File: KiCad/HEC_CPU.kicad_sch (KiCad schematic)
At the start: 20 parts, among them J3 Conn_02x05_Odd_Even, J9 Conn_02x14_Odd_Even, SW2 SW_Push, U1 Z80CPU, U16 74LS32, U20 74LS574, U21 74LS574, U22 74LS02, U30 74LS74, U34 74LS393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

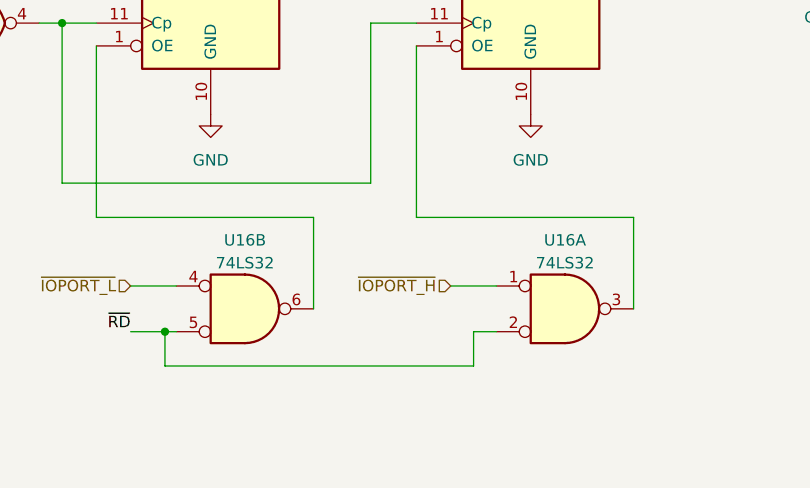
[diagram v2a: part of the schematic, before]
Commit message: Preliminary routing
Changed footprint pad size to allow 2 traces to be routed between adjacent pads. Finished routing all ICs. Bypass caps not added. Some traces may need to be optimized.
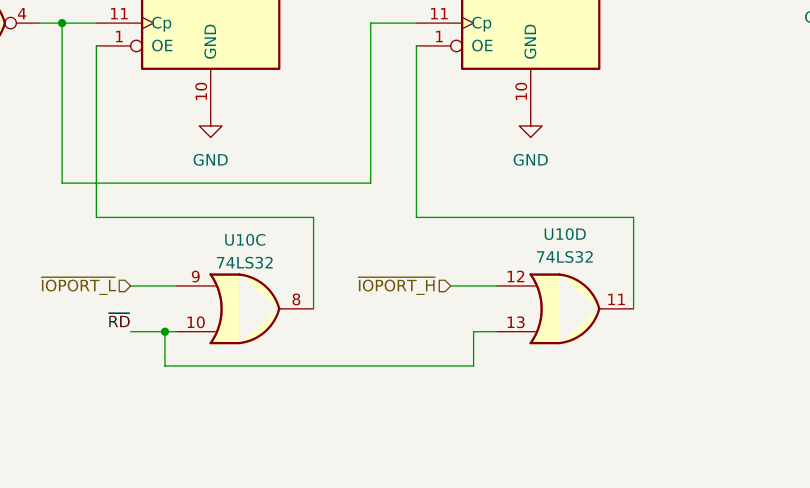
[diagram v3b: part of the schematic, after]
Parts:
- removed U16: 74LS32, Package_DIP:DIP-14_W7.62mm_Socket, symbol 74xx:74LS32
- added U10: 74LS32, Library:DIP-14_W7.62mm_Socket_ThinPads, symbol 74xx:74LS32
- U1: footprint Package_DIP:DIP-40_W15.24mm_Socket -> Library:DIP-40_W15.24mm_Socket_ThinPads
- U20, U21, U36: footprint Package_DIP:DIP-20_W7.62mm_Socket -> Library:DIP-20_W7.62mm_Socket_ThinPads
- U22, U30, U34, U37: footprint Package_DIP:DIP-14_W7.62mm_Socket -> Library:DIP-14_W7.62mm_Socket_ThinPads
- U38, U39: footprint Package_DIP:DIP-16_W7.62mm_Socket -> Library:DIP-16_W7.62mm_Socket_ThinPads
- U7: footprint Package_DIP:DIP-28_W15.24mm_Socket -> Library:DIP-28_W15.24mm_Socket_ThinPads
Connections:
- net ~{IOPORT_H}: now also U10.12
- net ~{IOPORT_L}: now also U10.9
- net ~{RD}: now also U10.10, U10.13
- net at U20.1 (OE): now also U10.8
- net at U21.1 (OE): now also U10.11
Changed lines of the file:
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@@
       (effects (font (size 1.27 1.27)) (justify left))
     )
-    (property "Footprint" "Package_DIP:DIP-16_W7.62mm_Socket" (at 205.105 77.47 0)
+    (property "Footprint" "Library:DIP-16_W7.62mm_Socket_ThinPads" (at 205.105 77.47 0)
       (effects (font (size 1.27 1.27)) hide)
     )
@@
       (effects (font (size 1.27 1.27)) (justify left))
     )
-    (property "Footprint" "Package_DIP:DIP-20_W7.62mm_Socket" (at 110.49 128.27 0)
+    (property "Footprint" "Library:DIP-20_W7.62mm_Socket_ThinPads" (at 110.49 128.27 0)
       (effects (font (size 1.27 1.27)) hide)
     )
@@
       (effects (font (size 1.27 1.27)) (justify left))
     )
-    (property "Footprint" "Package_DIP:DIP-20_W7.62mm_Socket" (at 168.91 52.07 0)
+    (property "Footprint" "Library:DIP-20_W7.62mm_Socket_ThinPads" (at 168.91 52.07 0)
       (effects (font (size 1.27 1.27)) hide)
     )
@@
     )
   )
+  (symbol (lib_id "74xx:74LS32") (at 114.3 170.18 0) (unit 3)
+    (in_bom yes) (on_board yes) (dnp no)
+    (property "Reference" "U10" (at 114.3 162.56 0)
+      (effects (font (size 1.27 1.27)))
+    )
+    (property "Value" "74LS32" (at 114.3 165.1 0)
+      (effects (font (size 1.27 1.27)))
+    )
+    (property "Footprint" "Library:DIP-14_W7.62mm_Socket_ThinPads" (at 114.3 170.18 0)
+      (effects (font (size 1.27 1.27)) hide)
+    )
+    (property "Datasheet" "http://www.ti.com/lit/gpn/sn74LS32" (at 114.3 170.18 0)
+      (effects (font (size 1.27 1.27)) hide)
+    )
+    (pin "1")
+    (pin "2")
+    (pin "3")
+    (pin "4")
+    (pin "5")
+    (pin "6")
+    (pin "10")
+    (pin "8")
+    (pin "9")
+    (pin "11")
+    (pin "12")
+    (pin "13")
+    (pin "14")
+    (pin "7")
+    (instances
+      (project "HEC1"
+        (path "/87935374-b60a-4f41-99da-94b76103dd77/73a0c68b-1e42-4c0d-ae31-b1a96d0648bb"
+          (reference "U10") (unit 3)
+        )
+        (path "/87935374-b60a-4f41-99da-94b76103dd77/2930b625-d6a3-4a7f-9d41-a454efcef99d"
+          (reference "U10") (unit 3)
+        )
+      )
+    )
+  )
   (symbol (lib_id "Oscillator:CXO_DIP8") (at 194.31 148.59 0) (unit 1)
     (in_bom yes) (on_board yes) (dnp no) (fields_autoplaced)
@@
       (effects (font (size 1.27 1.27)))
     )
-    (property "Footprint" "Package_DIP:DIP-14_W7.62mm_Socket" (at 147.32 99.06 0)
+    (property "Footprint" "Library:DIP-14_W7.62mm_Socket_ThinPads" (at 147.32 99.06 0)
       (effects (font (size 1.27 1.27)) hide)
     )
@@
       (effects (font (size 1.27 1.27)))
     )
-    (property "Footprint" "Package_DIP:DIP-14_W7.62mm_Socket" (at 83.82 138.43 0)
+    (property "Footprint" "Library:DIP-14_W7.62mm_Socket_ThinPads" (at 83.82 138.43 0)
       (effects (font (size 1.27 1.27)) hide)
     )
@@
       (effects (font (size 1.27 1.27)))
     )
-    (property "Footprint" "Package_DIP:DIP-14_W7.62mm_Socket" (at 231.775 151.13 0)
+    (property "Footprint" "Library:DIP-14_W7.62mm_Socket_ThinPads" (at 231.775 151.13 0)
       (effects (font (size 1.27 1.27)) hide)
     )
@@
       (effects (font (size 1.27 1.27)) (justify left))
     )
-    (property "Footprint" "Package_DIP:DIP-28_W15.24mm_Socket" (at 128.905 47.625 0)
+    (property "Footprint" "Library:DIP-28_W15.24mm_Socket_ThinPads" (at 128.905 47.625 0)
       (effects (font (size 1.27 1.27)) hide)
     )
@@
       (effects (font (size 1.27 1.27)) (justify left))
     )
-    (property "Footprint" "Package_DIP:DIP-20_W7.62mm_Socket" (at 146.05 128.27 0)
+    (property "Footprint" "Library:DIP-20_W7.62mm_Socket_ThinPads" (at 146.05 128.27 0)
       (effects (font (size 1.27 1.27)) hide)
     )
@@
       (effects (font (size 1.27 1.27)) (justify left))
     )
-    (property "Footprint" "Package_DIP:DIP-14_W7.62mm_Socket" (at 101.6 84.455 0)
+    (property "Footprint" "Library:DIP-14_W7.62mm_Socket_ThinPads" (at 101.6 84.455 0)
       (effects (font (size 1.27 1.27)) hide)
     )
@@
       (effects (font (size 1.27 1.27)))
     )
-    (property "Footprint" "Package_DIP:DIP-14_W7.62mm_Socket" (at 49.53 119.38 0)
+    (property "Footprint" "Library:DIP-14_W7.62mm_Socket_ThinPads" (at 49.53 119.38 0)
       (effects (font (size 1.27 1.27)) hide)
     )
@@
       (effects (font (size 1.27 1.27)))
     )
-    (property "Footprint" "Package_DIP:DIP-14_W7.62mm_Socket" (at 116.84 95.25 0)
+    (property "Footprint" "Library:DIP-14_W7.62mm_Socket_ThinPads" (at 116.84 95.25 0)
       (effects (font (size 1.27 1.27)) hide)
     )
@@
       (effects (font (size 1.27 1.27)))
     )
-    (property "Footprint" "Package_DIP:DIP-14_W7.62mm_Socket" (at 158.115 23.495 0)
+    (property "Footprint" "Library:DIP-14_W7.62mm_Socket_ThinPads" (at 158.115 23.495 0)
       (effects (font (size 1.27 1.27)) hide)
     )
@@
         (path "/87935374-b60a-4f41-99da-94b76103dd77/73a0c68b-1e42-4c0d-ae31-b1a96d0648bb"
           (reference "U37") (unit 2)
+        )
+      )
+    )
+  )
+  (symbol (lib_id "74xx:74LS32") (at 149.86 170.18 0) (unit 4)
+    (in_bom yes) (on_board yes) (dnp no) (fields_autoplaced)
+    (property "Reference" "U10" (at 149.86 161.925 0)
+      (effects (font (size 1.27 1.27)))
+    )
+    (property "Value" "74LS32" (at 149.86 164.465 0)
+      (effects (font (size 1.27 1.27)))
+    )
+    (property "Footprint" "Library:DIP-14_W7.62mm_Socket_ThinPads" (at 149.86 170.18 0)
+      (effects (font (size 1.27 1.27)) hide)
+    )
+    (property "Datasheet" "http://www.ti.com/lit/gpn/sn74LS32" (at 149.86 170.18 0)
+      (effects (font (size 1.27 1.27)) hide)
+    )
+    (pin "1")
+    (pin "2")
+    (pin "3")
+    (pin "4")
+    (pin "5")
+    (pin "6")
+    (pin "10")
+    (pin "8")
+    (pin "9")
+    (pin "11")
+    (pin "12")
+    (pin "13")
+    (pin "14")
+    (pin "7")
+    (instances
+      (project "HEC1"
+        (path "/87935374-b60a-4f41-99da-94b76103dd77/933a6f90-eb98-4eb1-8c19-8a76228aece1"
+          (reference "U10") (unit 4)
+        )
+        (path "/87935374-b60a-4f41-99da-94b76103dd77/2930b625-d6a3-4a7f-9d41-a454efcef99d"
+          (reference "U10") (unit 4)
+        )
+        (path "/87935374-b60a-4f41-99da-94b76103dd77/73a0c68b-1e42-4c0d-ae31-b1a96d0648bb"
+          (reference "U10") (unit 4)
         )
       )
@@
     )
   )
-  (symbol (lib_id "74xx:74LS32") (at 114.3 170.18 0) (unit 2) (convert 2)
-    (in_bom yes) (on_board yes) (dnp no) (fields_autoplaced)
-    (property "Reference" "U16" (at 114.3 162.56 0)
-      (effects (font (size 1.27 1.27)))
-    )
-    (property "Value" "74LS32" (at 114.3 165.1 0)
-      (effects (font (size 1.27 1.27)))
-    )
-    (property "Footprint" "Package_DIP:DIP-14_W7.62mm_Socket" (at 114.3 170.18 0)
-      (effects (font (size 1.27 1.27)) hide)
-    )
-    (property "Datasheet" "http://www.ti.com/lit/gpn/sn74LS32" (at 114.3 170.18 0)
-      (effects (font (size 1.27 1.27)) hide)
-    )
-    (pin "1")
-    (pin "2")
-    (pin "3")
-    (pin "4")
-    (pin "5")
-    (pin "6")
-    (pin "10")
-    (pin "8")
-    (pin "9")
-    (pin "11")
-    (pin "12")
-    (pin "13")
-    (pin "14")
-    (pin "7")
-    (instances
-      (project "HEC1"
-        (path "/87935374-b60a-4f41-99da-94b76103dd77/933a6f90-eb98-4eb1-8c19-8a76228aece1"
-          (reference "U16") (unit 2)
-        )
-        (path "/87935374-b60a-4f41-99da-94b76103dd77/73a0c68b-1e42-4c0d-ae31-b1a96d0648bb"
-          (reference "U16") (unit 2)
-        )
-      )
-    )
-  )
   (symbol (lib_id "power:VCC") (at 194.31 140.97 0) (unit 1)
     (in_bom yes) (on_board yes) (dnp no) (fields_autoplaced)
@@
       (effects (font (size 1.27 1.27)) (justify left))
     )
-    (property "Footprint" "Package_DIP:DIP-16_W7.62mm_Socket" (at 205.105 33.02 0)
+    (property "Footprint" "Library:DIP-16_W7.62mm_Socket_ThinPads" (at 205.105 33.02 0)
       (effects (font (size 1.27 1.27)) hide)
     )
@@
       (effects (font (size 1.27 1.27)) (justify left))
     )
-    (property "Footprint" "Package_DIP:DIP-40_W15.24mm_Socket" (at 46.99 44.45 0)
+    (property "Footprint" "Library:DIP-40_W15.24mm_Socket_ThinPads" (at 46.99 44.45 0)
       (effects (font (size 1.27 1.27)) hide)
     )
@@
       (effects (font (size 1.27 1.27)) (justify left))
     )
-    (property "Footprint" "Package_DIP:DIP-14_W7.62mm_Socket" (at 50.165 167.005 0)
+    (property "Footprint" "Library:DIP-14_W7.62mm_Socket_ThinPads" (at 50.165 167.005 0)
       (effects (font (size 1.27 1.27)) hide)
     )
@@
     )
   )
-  (symbol (lib_id "74xx:74LS32") (at 149.86 170.18 0) (unit 1) (convert 2)
-    (in_bom yes) (on_board yes) (dnp no) (fields_autoplaced)
-    (property "Reference" "U16" (at 149.86 162.56 0)
-      (effects (font (size 1.27 1.27)))
-    )
-    (property "Value" "74LS32" (at 149.86 165.1 0)
-      (effects (font (size 1.27 1.27)))
-    )
-    (property "Footprint" "Package_DIP:DIP-14_W7.62mm_Socket" (at 149.86 170.18 0)
-      (effects (font (size 1.27 1.27)) hide)
-    )
-    (property "Datasheet" "http://www.ti.com/lit/gpn/sn74LS32" (at 149.86 170.18 0)
-      (effects (font (size 1.27 1.27)) hide)
-    )
-    (pin "1")
-    (pin "2")
-    (pin "3")
-    (pin "4")
-    (pin "5")
-    (pin "6")
-    (pin "10")
-    (pin "8")
-    (pin "9")
-    (pin "11")
-    (pin "12")
-    (pin "13")
-    (pin "14")
-    (pin "7")
-    (instances
-      (project "HEC1"
-        (path "/87935374-b60a-4f41-99da-94b76103dd77/933a6f90-eb98-4eb1-8c19-8a76228aece1"
-          (reference "U16") (unit 1)
-        )
-        (path "/87935374-b60a-4f41-99da-94b76103dd77/73a0c68b-1e42-4c0d-ae31-b1a96d0648bb"
-          (reference "U16") (unit 1)
-        )
-      )
-    )
-  )
   (symbol (lib_id "power:VCC") (at 50.165 154.305 0) (unit 1)
     (in_bom yes) (on_board yes) (dnp no) (fields_autoplaced)
@@
       (effects (font (size 1.27 1.27)) (justify left))
     )
-    (property "Footprint" "Package_DIP:DIP-14_W7.62mm_Socket" (at 73.66 168.91 0)
-      (effects (font (size 1.27 1.27)) hide)
-    )
+    (property "Footprint" "Library:DIP-14_W7.62mm_Socket_ThinPads" (at 73.66 168.91 0)
+      (effects (font (size 1.27 1.27)) hide)
+    )
